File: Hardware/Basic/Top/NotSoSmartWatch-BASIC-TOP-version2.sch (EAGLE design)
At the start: 50 parts, among them SW3 SWITCH.MOM, SW4 SWITCH.MOM, U1 NRF52832_MODULE_MDBT42

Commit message: almost done with Take 007
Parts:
- C17: device LinnesLab-Passives:CAPACITOR0402 -> LinnesLab-Passives:CAPACITOR0603
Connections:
- net !CTS renamed CTS
- removed net !DTR: FTDI.!DTR
- removed net A4/VBATT: R8.1, R9.2, U1.P0.28/AIN4
- removed net A6/TIA: U1.P0.30/AIN6
- removed net A7/PPG: U1.P0.31/AIN7
- removed net D29/LED.CTRL: U1.P0.29/AIN5
- removed net N$21: J1.5
- removed net N$22: J1.4
- removed net N$27: J1.3
- removed net N$28: J1.2
- removed net N$29: J1.1
- new net A4/PPG: J1.7, U1.P0.28/AIN4
- new net A5/TIA: J1.6, U1.P0.29/AIN5
- new net A7/BATT: R8.1, R9.2, U1.P0.31/AIN7
- new net D30/LED.CTRL: J1.5, U1.P0.30/AIN6
- net 3.3V: now also J1.4; no longer J1.7
- net DTR: now also FTDI.!DTR
- net GND: now also J1.3; no longer J1.6
- net SCL: now also J1.2
- net SDA: now also J1.1

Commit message: updated through Take 007
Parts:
- added C5, C7: 4.7u, LinnesLab-Passives:CAPACITOR0603
- added C8, C9: 1u, LinnesLab-Passives:CAPACITOR0603
- added CHRG: MCP73831, LinnesLab-Power:MCP73831
- added LDO1: MIC5504, LinnesLab-Power:MIC5504
- added R3, R7: 100k, LinnesLab-Passives:RESISTOR0603
- added R6: (no value), LinnesLab-Passives:RESISTOR0603
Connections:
- new net N$16: CHRG.PROG, R6.2
- net 3.3V: now also C9.1, LDO1.OUT, R7.2
- net D27/CHRG.STAT: now also CHRG.STAT, R3.1
- net GND: now also C5.2, C7.1, C8.1, C9.2, CHRG.VSS, LDO1.GND, R6.1, R7.1
- net VIN: now also C7.2, C8.2, CHRG.VIN, LDO1.EN, LDO1.IN, R3.2
- net VLIPO: now also C5.1, CHRG.VBAT

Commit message: updated through Take 008
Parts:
- R6: value (none) -> 5k
- renumbered SW2 to RESET
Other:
- note added: "Diodes switch from LiPo power to USB when USB is connected the USB then charges the battery"
- note added: "R6 sets charge current i_charge = 1000V/R6 per MP73831 datasheet"
- note added: "Voltage divider used to monitor battery voltage"
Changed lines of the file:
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@@
 <part name="SW1" library="LinnesLab-Switches" deviceset="SPST-PTS830GG140-COPY" device=".1-3" package3d_urn="urn:adsk.eagle:package:18580190/2"/>
 <part name="GND30" library="LinnesLab-Symbols" deviceset="GND" device=""/>
-<part name="SW2" library="LinnesLab-Switches" deviceset="SPST-PTS830GG140-COPY" device=".1-3" package3d_urn="urn:adsk.eagle:package:18580190/2"/>
+<part name="RESET" library="LinnesLab-Switches" deviceset="SPST-PTS830GG140-COPY" device=".1-3" package3d_urn="urn:adsk.eagle:package:18580190/2"/>
 <part name="U1" library="LinnesLab-Microcontrollers" deviceset="NRF52832_MODULE_MDBT42" device="" override_package3d_urn="urn:adsk.eagle:package:18593121/2" override_package_urn="urn:adsk.eagle:footprint:18593122/1"/>
 <part name="LED1" library="LinnesLab-LED" deviceset="LED" device="0603" package3d_urn="urn:adsk.eagle:package:18593052/2" value="RED"/>
@@
 <part name="C5" library="LinnesLab-Passives" deviceset="CAPACITOR" device="0603" package3d_urn="urn:adsk.eagle:package:15661989/2" value="4.7u"/>
 <part name="C7" library="LinnesLab-Passives" deviceset="CAPACITOR" device="0603" package3d_urn="urn:adsk.eagle:package:15661989/2" value="4.7u"/>
-<part name="R6" library="LinnesLab-Passives" deviceset="RESISTOR" device="0603" package3d_urn="urn:adsk.eagle:package:15661944/2"/>
+<part name="R6" library="LinnesLab-Passives" deviceset="RESISTOR" device="0603" package3d_urn="urn:adsk.eagle:package:15661944/2" value="5k"/>
 <part name="R3" library="LinnesLab-Passives" deviceset="RESISTOR" device="0603" package3d_urn="urn:adsk.eagle:package:15661944/2" value="100k"/>
 <part name="GND34" library="LinnesLab-Symbols" deviceset="GND" device=""/>
@@
 <wire x1="81.28" y1="215.9" x2="81.28" y2="314.96" width="1.27" layer="97" style="longdash"/>
 <wire x1="81.28" y1="314.96" x2="83.82" y2="314.96" width="1.27" layer="97" style="longdash"/>
+<text x="15.24" y="-12.7" size="1.778" layer="97">Diodes switch from LiPo power
+to USB when USB is connected
+the USB then charges the battery</text>
+<text x="167.64" y="-76.2" size="1.778" layer="97">R6 sets charge current
+i_charge = 1000V/R6
+per MP73831 datasheet</text>
+<text x="172.72" y="-7.62" size="1.778" layer="97">Voltage divider used to
+monitor battery voltage</text>
 </plain>
 <instances>
@@
 <attribute name="VALUE" x="71.12" y="78.486" size="1.778" layer="96" align="top-center"/>
 </instance>
-<instance part="SW2" gate="G$1" x="261.62" y="48.26" smashed="yes">
+<instance part="RESET" gate="G$1" x="261.62" y="48.26" smashed="yes">
 <attribute name="NAME" x="259.08" y="45.72" size="1.27" layer="95"/>
 <attribute name="VALUE" x="259.08" y="43.18" size="1.27" layer="96"/>
@@
 <wire x1="269.24" y1="48.26" x2="269.24" y2="45.72" width="0.1524" layer="91"/>
 <pinref part="GND28" gate="G$1" pin="GND"/>
-<pinref part="SW2" gate="G$1" pin="B"/>
+<pinref part="RESET" gate="G$1" pin="B"/>
 </segment>
 <segment>
@@
 <wire x1="254" y1="48.26" x2="256.54" y2="48.26" width="0.1524" layer="91"/>
 <label x="254" y="48.26" size="1.27" layer="95" rot="R180" xref="yes"/>
-<pinref part="SW2" gate="G$1" pin="A"/>
-</segment>
-<segment>
+<pinref part="RESET" gate="G$1" pin="A"/>
+</segment>
+<segment>

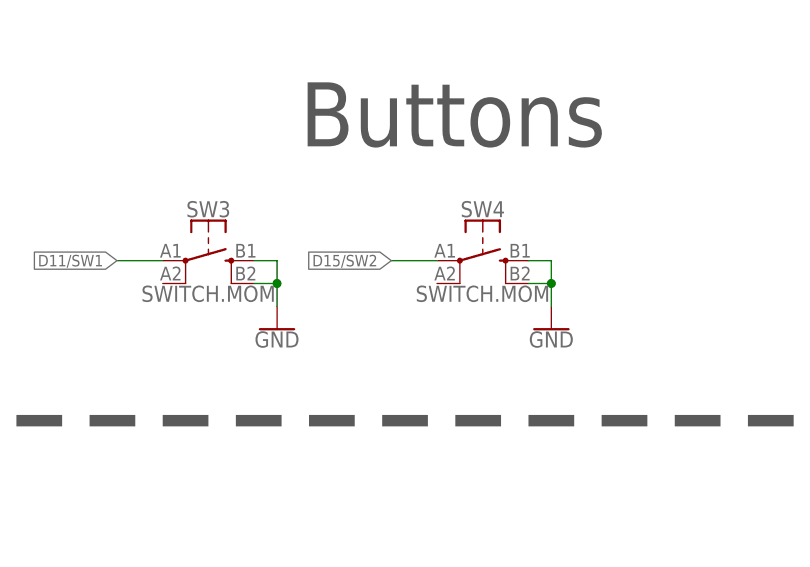
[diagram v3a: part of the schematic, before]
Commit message: fixed ground connections on buttons - should be good now
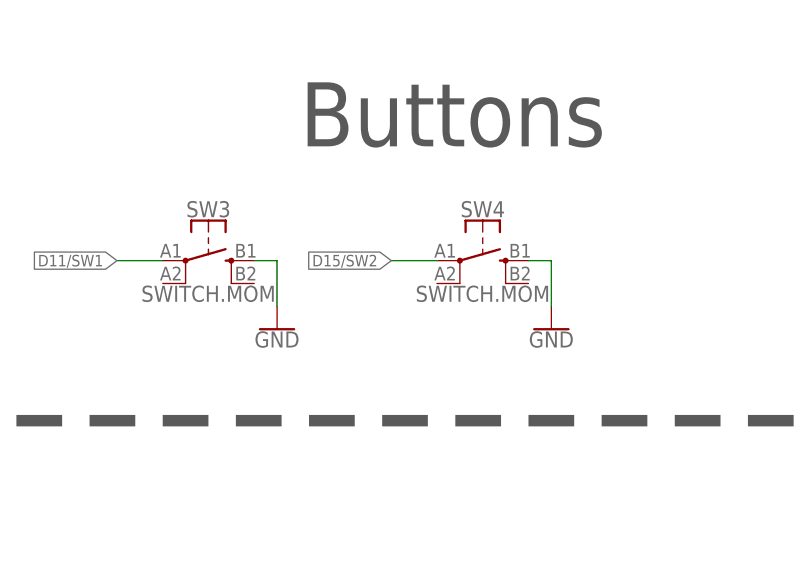
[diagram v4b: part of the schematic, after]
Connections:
- net GND: no longer SW3.4, SW4.4
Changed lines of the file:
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@@
 <pinref part="SW3" gate="G$1" pin="3"/>
 <wire x1="363.22" y1="2.54" x2="365.76" y2="2.54" width="0.1524" layer="91"/>
-<wire x1="365.76" y1="2.54" x2="365.76" y2="0" width="0.1524" layer="91"/>
-<pinref part="SW3" gate="G$1" pin="4"/>
-<wire x1="365.76" y1="0" x2="365.76" y2="-2.54" width="0.1524" layer="91"/>
-<wire x1="363.22" y1="0" x2="365.76" y2="0" width="0.1524" layer="91"/>
-<junction x="365.76" y="0"/>
+<wire x1="365.76" y1="2.54" x2="365.76" y2="-2.54" width="0.1524" layer="91"/>
 <pinref part="GND1" gate="G$1" pin="GND"/>
 </segment>
@@
 <pinref part="SW4" gate="G$1" pin="3"/>
 <wire x1="393.7" y1="2.54" x2="396.24" y2="2.54" width="0.1524" layer="91"/>
-<wire x1="396.24" y1="2.54" x2="396.24" y2="0" width="0.1524" layer="91"/>
-<pinref part="SW4" gate="G$1" pin="4"/>
-<wire x1="396.24" y1="0" x2="396.24" y2="-2.54" width="0.1524" layer="91"/>
-<wire x1="393.7" y1="0" x2="396.24" y2="0" width="0.1524" layer="91"/>
-<junction x="396.24" y="0"/>
+<wire x1="396.24" y1="2.54" x2="396.24" y2="-2.54" width="0.1524" layer="91"/>
 <pinref part="GND3" gate="G$1" pin="GND"/>
 </segment>
